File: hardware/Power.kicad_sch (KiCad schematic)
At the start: 51 parts, among them U10 LDK320ADU120R, U4 TPS563300DRLR, U5 TPS563219ADDFR, U6 LM2940CS-12/NOPB, U7 LM1117IMP-5.0, U8 TPS7B92033DBVR, U9 AP2127N3-1.5

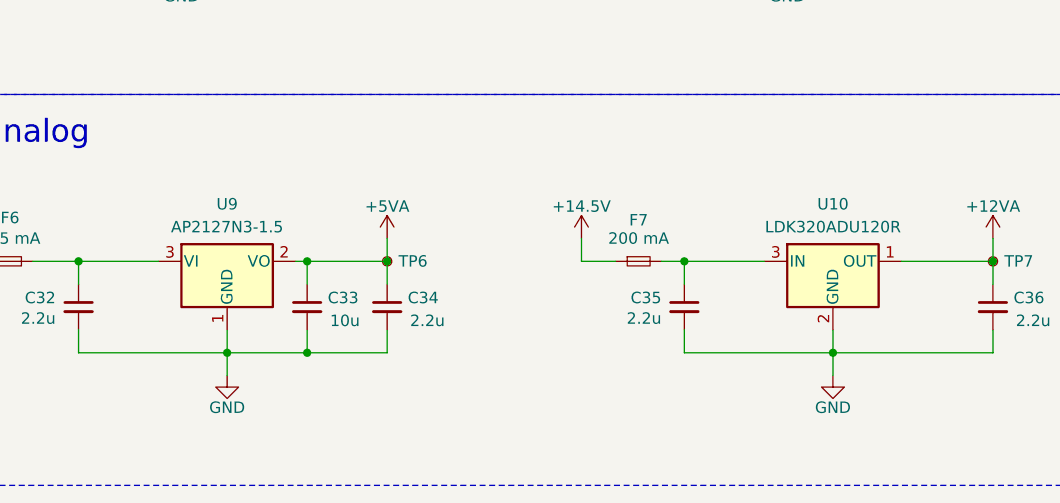
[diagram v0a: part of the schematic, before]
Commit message: Fixed pinout errors & changed branch name
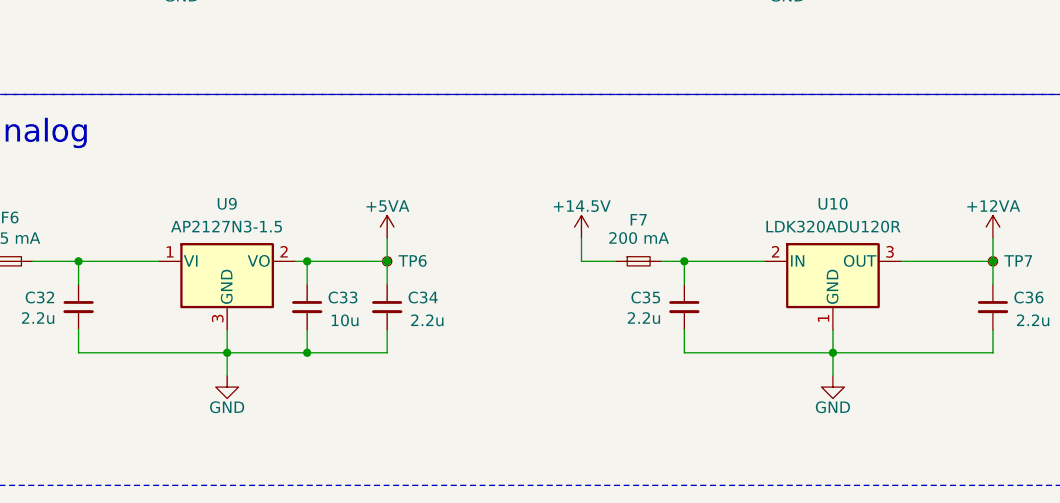
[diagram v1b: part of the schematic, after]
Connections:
- net +12VA: now also U10.3 (OUT); no longer U10.1 (OUT)
- net GND: now also U10.1 (GND), U9.3 (GND); no longer U10.2 (GND), U9.1 (GND)
- net at C35.1, F7.2: now also U10.2 (IN); no longer U10.3 (IN)
- net at C32.1, F6.2: now also U9.1 (VI); no longer U9.3 (VI)
